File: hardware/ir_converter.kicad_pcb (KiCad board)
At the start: 2 copper layers, 33.5 x 49.5 mm, 140 parts, among them J1 MX-47346-0001, J2 SWD, J3 TP, J4 TP, Q1 LL-S350PTC-1A, Q2 BC817-40, SW1 RESET, SW2 SW2, U1 TLV70033DDCT, U2 USBLC6-2, U3 STM32F103C8T6

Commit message: Prepared for fabrication
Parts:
- added REF**: MountingHole_1mm, CustomFootprints:MountingHole_1mm, F.Cu at (112.8, 136.7)
- added REF**: MountingHole_1mm, CustomFootprints:MountingHole_1mm, F.Cu at (83.2, 102.4)
- added REF**: MountingHole_2mm, CustomFootprints:MountingHole_2mm, F.Cu at (111.1, 91.7)
- added REF**: MountingHole_2.75mm, CustomFootprints:MountingHole_2.75mm, F.Cu at (102.5, 91.7)
- added REF**: MountingHole_2mm, CustomFootprints:MountingHole_2mm, F.Cu at (102.0, 112.3)
- added REF**: MountingHole_1mm, CustomFootprints:MountingHole_1mm, F.Cu at (112.8, 102.4)
- Q1: footprint CustomFootprints:IR_PHOTO_WIDE -> IR_PHOTO_WIDE
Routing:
- net +3V3: track 148.0 -> 149.8 mm, vias 25 -> 21
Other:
- outline, holes or cut-outs redrawn

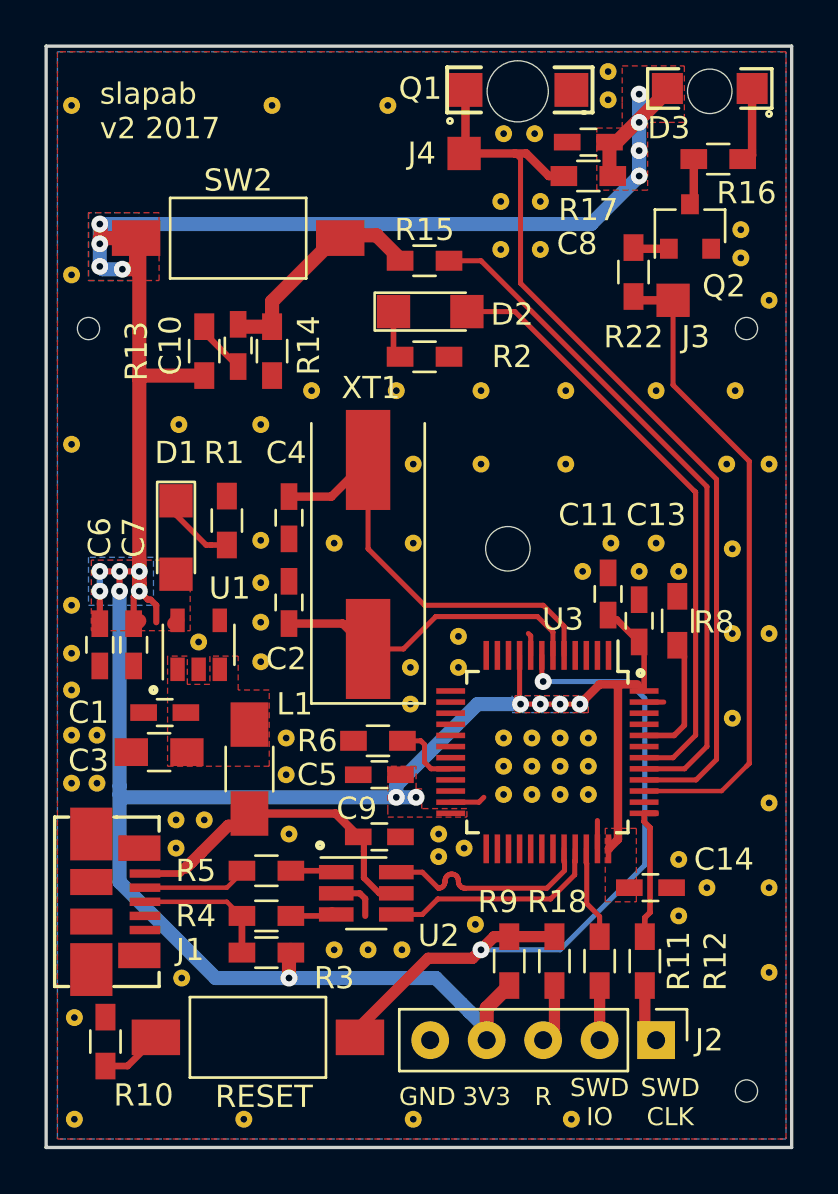
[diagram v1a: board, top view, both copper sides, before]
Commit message: Resizing mouting holes
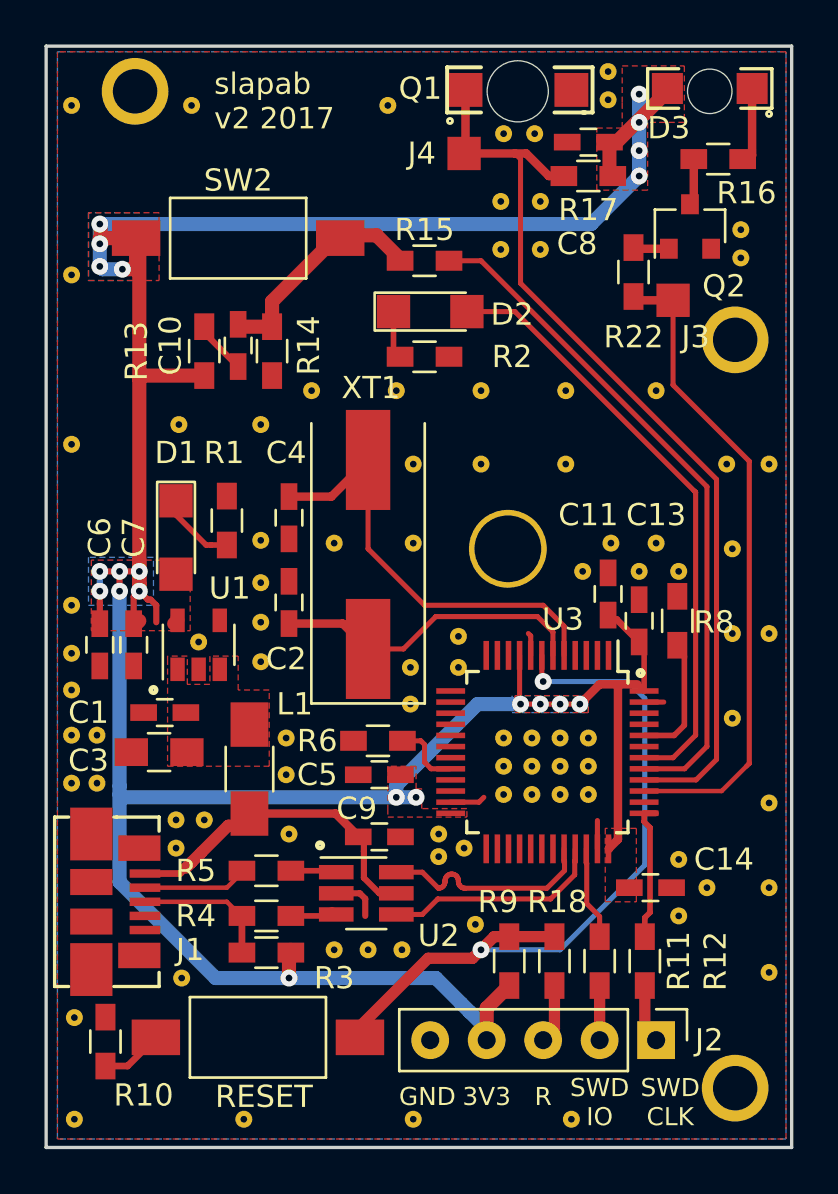
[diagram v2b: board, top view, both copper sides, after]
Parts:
- removed the REF** at (113.8, 101.1)
- removed the REF** at (112.3, 105.2)
- REF**: footprint CustomFootprints:MountingHole_2mm -> MountingHole_3mm
- REF**: footprint CustomFootprints:MountingHole_1mm -> MountingHole_2mm
- REF** (x2): footprint CustomFootprints:MountingHole_1mm -> CustomFootprints:MountingHole_2mm
- moved REF** 10.9 mm to (85.3, 91.7)
- moved REF** 3.62 mm to (87.8, 92.3)
- moved REF** 0.72 mm to (112.3, 102.9)
- moved REF** 0.52 mm to (112.3, 136.5)
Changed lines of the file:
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@@
 (kicad_pcb (version 4) (host pcbnew 4.0.6)
   (general
-    (links 190)
+    (links 188)
     (no_connects 0)
     (area 35.330001 62.738 157.757715 167.800001)
@@
     (tracks 313)
     (zones 0)
-    (modules 146)
+    (modules 144)
     (nets 61)
   )
@@
     (visible_elements FFFFFF6F)
     (pcbplotparams
-      (layerselection 0x010f0_80000001)
+      (layerselection 0x290f0_80000001)
       (usegerberextensions true)
       (gerberprecision 5)
@@
     (add_net +3V3)
   )
-  (module IR_PHOTO_WIDE (layer F.Cu)
+  (module MountingHole_3mm locked (layer F.Cu)
+    (at 102.0445 112.268)
+    (tags "mounting hole 3mm no annular")
+    (fp_text reference REF** (at 0.1905 -2.54) (layer Dwgs.User) hide
+      (effects (font (size 1 1) (thickness 0.15)))
+    )
+    (fp_text value MountingHole_2mm (at 0 2.54) (layer F.Fab) hide
+      (effects (font (size 1 1) (thickness 0.15)))
+    )
+    (fp_circle (center 0 0) (end 0.9525 0) (layer Cmts.User) (width 0.15))
+    (fp_circle (center 0 0) (end 1.0795 0) (layer F.CrtYd) (width 0.05))
+    (pad "" np_thru_hole circle (at 0 0) (size 3.5 3.5) (drill 3) (layers *.Cu *.Mask))
+  )
+  (module MountingHole_2mm locked (layer F.Cu)
+    (at 112.268 102.87)
+    (tags "mounting hole 2mm no annular")
+    (fp_text reference REF** (at 0 -2.54) (layer Dwgs.User) hide
+      (effects (font (size 1 1) (thickness 0.15)))
+    )
+    (fp_text value MountingHole_1mm (at 0 2.54) (layer F.Fab) hide
+      (effects (font (size 1 1) (thickness 0.15)))
+    )
+    (fp_circle (center 0 0) (end 0.4445 0) (layer Cmts.User) (width 0.15))
+    (fp_circle (center 0 0) (end 0.508 0) (layer F.CrtYd) (width 0.05))
+    (pad "" np_thru_hole circle (at 0 0) (size 3 3) (drill 2) (layers *.Cu *.Mask))
+  )
+  (module IR_PHOTO_WIDE locked (layer F.Cu)
     (at 102.489 91.6305 180)
     (fp_text reference Q1 (at 4.3815 0.0635 180) (layer F.SilkS)
@@
     )
   )
-  (module CustomFootprints:MountingHole_1mm locked (layer F.Cu)
-    (at 112.776 136.652)
-    (tags "mounting hole 2.5mm no annular")
-    (fp_text reference REF** (at 0 -1.3335) (layer Dwgs.User) hide
-      (effects (font (size 1 1) (thickness 0.15)))
-    )
-    (fp_text value MountingHole_1mm (at 0 1.2065) (layer F.Fab) hide
-      (effects (font (size 1 1) (thickness 0.15)))
-    )
-    (fp_circle (center 0 0) (end 0.4445 0) (layer Cmts.User) (width 0.15))
-    (fp_circle (center 0 0) (end 0.508 0) (layer F.CrtYd) (width 0.05))
-    (pad "" np_thru_hole circle (at 0 0) (size 1 1) (drill 1) (layers *.Cu *.Mask))
-  )
-  (module CustomFootprints:MountingHole_1mm locked (layer F.Cu)
-    (at 83.185 102.362)
-    (tags "mounting hole 2.5mm no annular")
-    (fp_text reference REF** (at 0 -1.3335) (layer Dwgs.User) hide
-      (effects (font (size 1 1) (thickness 0.15)))
-    )
-    (fp_text value MountingHole_1mm (at 0 1.2065) (layer F.Fab) hide
-      (effects (font (size 1 1) (thickness 0.15)))
-    )
-    (fp_circle (center 0 0) (end 0.4445 0) (layer Cmts.User) (width 0.15))
-    (fp_circle (center 0 0) (end 0.508 0) (layer F.CrtYd) (width 0.05))
-    (pad "" np_thru_hole circle (at 0 0) (size 1 1) (drill 1) (layers *.Cu *.Mask))
-  )
   (module CustomFootprints:VIA_03_30mil (layer F.Cu)
     (at 94.234 112.014)
@@
   )
   (module CustomFootprints:VIA_03_30mil (layer F.Cu)
-    (at 91.44 92.329)
+    (at 87.8205 92.329)
     (fp_text reference REF** (at 0.254 -1.016) (layer F.SilkS) hide
       (effects (font (size 1 1) (thickness 0.15)))
@@
   )
   (module CustomFootprints:VIA_03_30mil (layer F.Cu)
-    (at 113.792 101.092)
-    (fp_text reference REF** (at 0.254 -1.016) (layer F.SilkS) hide
-      (effects (font (size 1 1) (thickness 0.15)))
-    )
-    (fp_text value VIA_03_30mil (at 0 1.016) (layer F.Fab) hide
-      (effects (font (size 1 1) (thickness 0.15)))
-    )
-    (pad 1 thru_hole circle (at 0 0) (size 0.762 0.762) (drill 0.3) (layers *.Cu)
-      (net 2 GND) (zone_connect 2))
-  )
-  (module CustomFootprints:VIA_03_30mil (layer F.Cu)
     (at 100.838 108.458)
     (fp_text reference REF** (at 0.254 -1.016) (layer F.SilkS) hide
@@
   )
   (module CustomFootprints:VIA_03_30mil (layer F.Cu)
-    (at 112.268 105.156)
-    (fp_text reference REF** (at 0.254 -1.016) (layer F.SilkS) hide
-      (effects (font (size 1 1) (thickness 0.15)))
-    )
-    (fp_text value VIA_03_30mil (at 0 1.016) (layer F.Fab) hide
-      (effects (font (size 1 1) (thickness 0.15)))
-    )
-    (pad 1 thru_hole circle (at 0 0) (size 0.762 0.762) (drill 0.3) (layers *.Cu)
-      (net 2 GND) (zone_connect 2))
-  )
-  (module CustomFootprints:VIA_03_30mil (layer F.Cu)
     (at 108.712 105.156)
     (fp_text reference REF** (at 0.254 -1.016) (layer F.SilkS) hide
@@
     )
   )
-  (module CustomFootprints:IR_LED_WIDE (layer F.Cu)
+  (module CustomFootprints:IR_LED_WIDE locked (layer F.Cu)
     (at 111.125 91.567 180)
     (fp_text reference D3 (at 1.8415 -1.778 180) (layer F.SilkS)
@@
   )
   (module CustomFootprints:MountingHole_2mm locked (layer F.Cu)
-    (at 102.0445 112.268)
-    (tags "mounting hole 2.5mm no annular")
-    (fp_text reference REF** (at 0.1905 -1.9685) (layer Dwgs.User) hide
+    (at 112.268 136.525)
+    (tags "mounting hole 2mm no annular")
+    (fp_text reference REF** (at 0 -2.54) (layer Dwgs.User) hide
       (effects (font (size 1 1) (thickness 0.15)))
     )
-    (fp_text value MountingHole_2mm (at 0 1.9685) (layer F.Fab) hide
+    (fp_text value MountingHole_1mm (at 0 2.54) (layer F.Fab) hide
       (effects (font (size 1 1) (thickness 0.15)))
     )
-    (fp_circle (center 0 0) (end 0.9525 0) (layer Cmts.User) (width 0.15))
-    (fp_circle (center 0 0) (end 1.0795 0) (layer F.CrtYd) (width 0.05))
-    (pad "" np_thru_hole circle (at 0 0) (size 2 2) (drill 2) (layers *.Cu *.Mask))
+    (fp_circle (center 0 0) (end 0.4445 0) (layer Cmts.User) (width 0.15))
+    (fp_circle (center 0 0) (end 0.508 0) (layer F.CrtYd) (width 0.05))
+    (pad "" np_thru_hole circle (at 0 0) (size 3 3) (drill 2) (layers *.Cu *.Mask))
   )
-  (module CustomFootprints:MountingHole_1mm locked (layer F.Cu)
-    (at 112.776 102.362)
-    (tags "mounting hole 2.5mm no annular")
-    (fp_text reference REF** (at 0 -1.3335) (layer Dwgs.User) hide
+  (module CustomFootprints:MountingHole_2mm (layer F.Cu)
+    (at 85.2805 91.694)
+    (tags "mounting hole 2mm no annular")
+    (fp_text reference REF** (at 0 -2.54) (layer Dwgs.User) hide
       (effects (font (size 1 1) (thickness 0.15)))
     )
-    (fp_text value MountingHole_1mm (at 0 1.2065) (layer F.Fab) hide
+    (fp_text value MountingHole_1mm (at 0 2.54) (layer F.Fab) hide
       (effects (font (size 1 1) (thickness 0.15)))
     )
     (fp_circle (center 0 0) (end 0.4445 0) (layer Cmts.User) (width 0.15))
     (fp_circle (center 0 0) (end 0.508 0) (layer F.CrtYd) (width 0.05))
-    (pad "" np_thru_hole circle (at 0 0) (size 1 1) (drill 1) (layers *.Cu *.Mask))
+    (pad "" np_thru_hole circle (at 0 0) (size 3 3) (drill 2) (layers *.Cu *.Mask))
   )
   (dimension 49.53 (width 0.3) (layer Dwgs.User)
@@
     (arrow2b (pts (xy 80.264 144.78) (xy 79.137496 145.366421)))
   )
-  (gr_text "slapab\nv2 2017" (at 83.693 92.583) (layer F.SilkS)
+  (gr_text "slapab\nv2 2017" (at 88.8365 92.1385) (layer F.SilkS)
     (effects (font (size 0.9652 0.9652) (thickness 0.2413)) (justify left))
   )
